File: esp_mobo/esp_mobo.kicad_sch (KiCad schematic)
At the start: 62 parts, among them J1 Conn_01x04_Pin, J10 Conn_01x03_Pin, J11 Conn_01x03_Pin, J12 Conn_01x03_Pin, J13 Conn_01x03_Pin, J14 Conn_01x03_Pin, J15 Conn_01x03_Pin, J2 Screw_Terminal_01x02, J3 Conn_01x03_Pin, J4 Conn_01x03_Pin, J5 Conn_01x03_Pin, J6 Conn_01x03_Pin, J7 Conn_01x03_Pin, J8 Conn_01x03_Pin, J9 Conn_01x03_Pin, U1 ESP32-DevKitC, U2 74AHCT125, U3 PC847, U4 PC847, U5 BME280

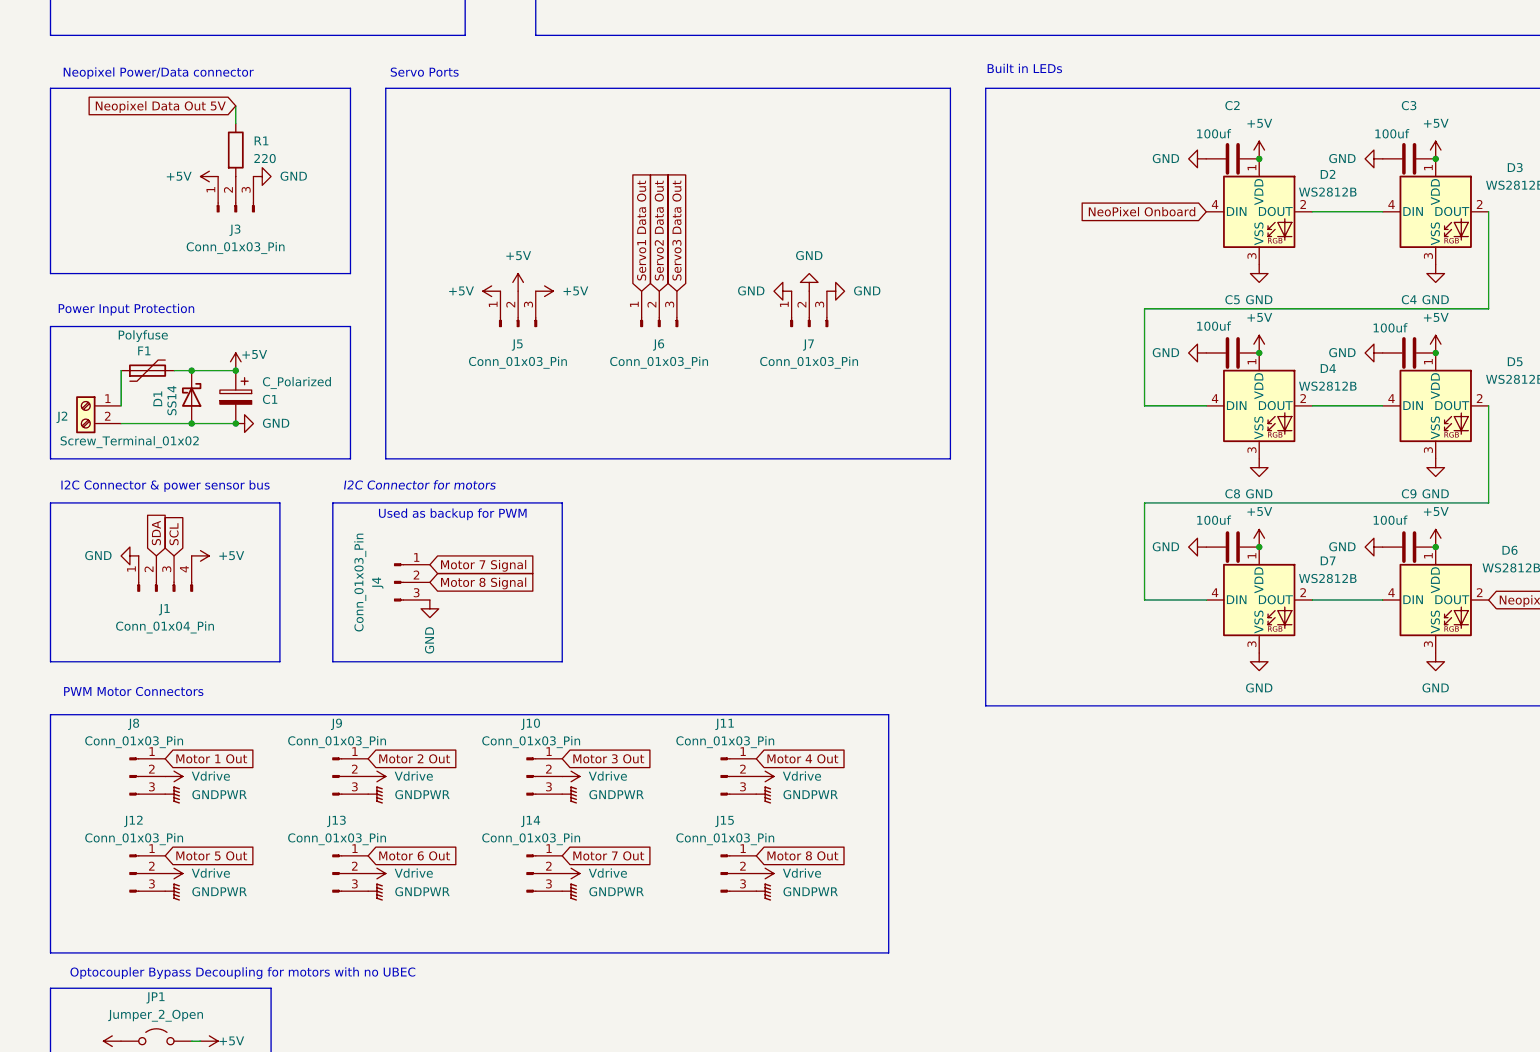
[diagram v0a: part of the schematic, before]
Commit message: Update ESC Mobo Silkscreen
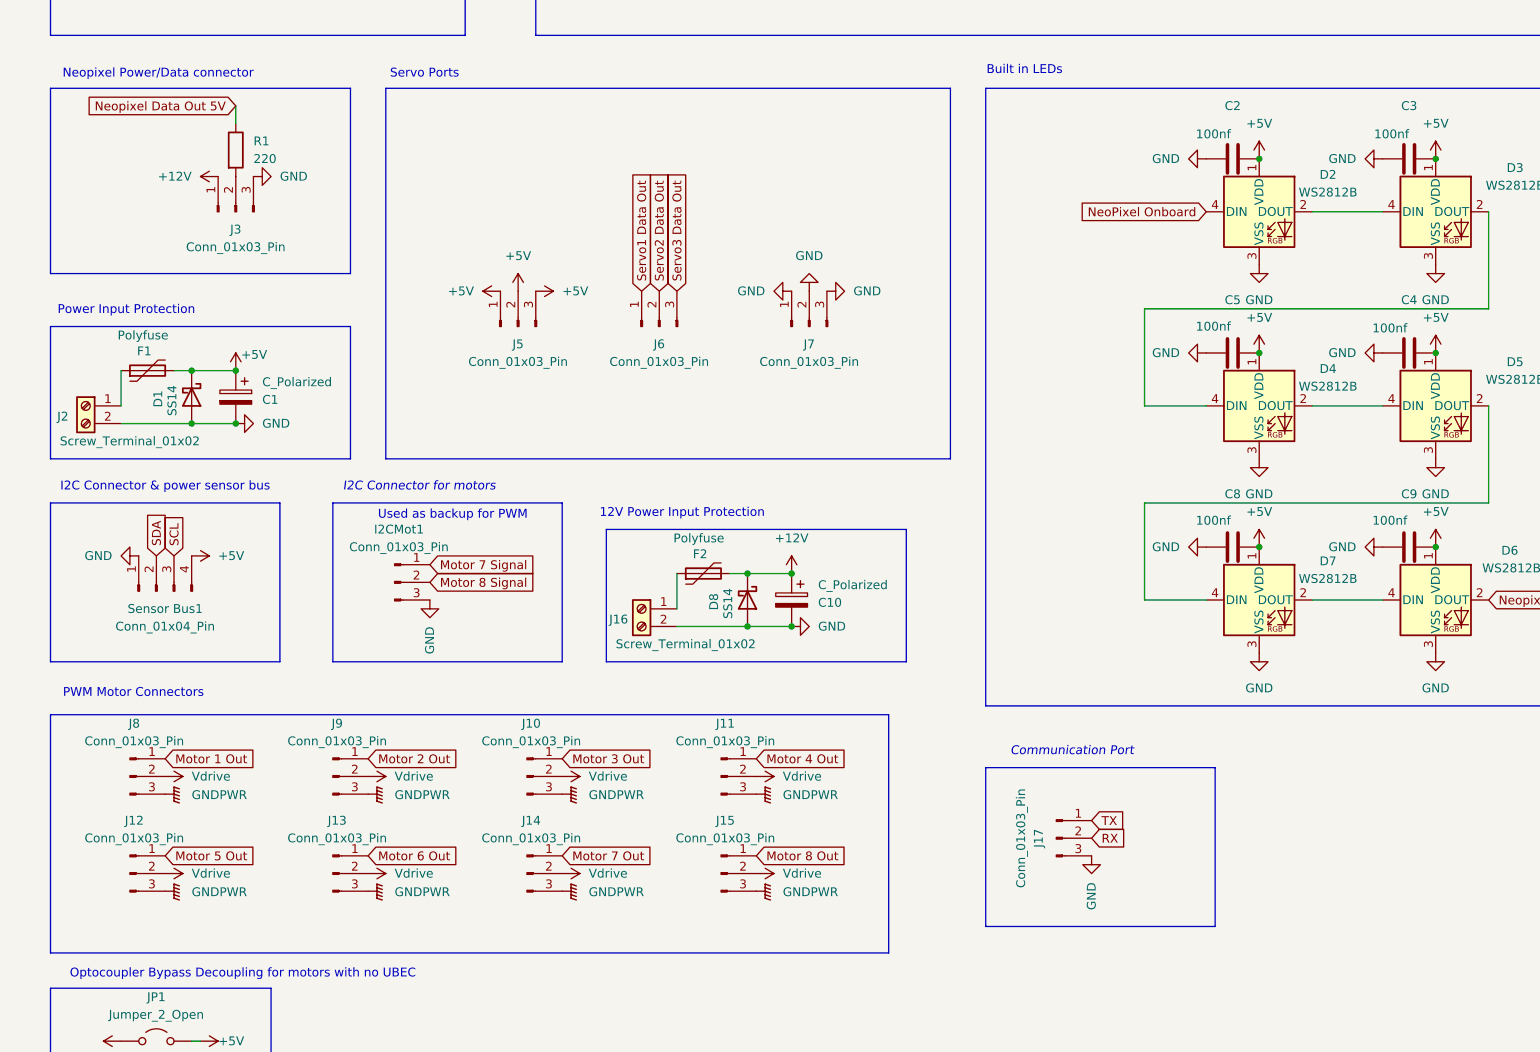
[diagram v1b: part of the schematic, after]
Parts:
- added C10: C_Polarized, Capacitor_THT:CP_Radial_D5.0mm_P2.00mm, symbol Device:C_Polarized
- added D8: SS14, Diode_SMD:D_SMA, symbol Diode:SS14
- added F2: Polyfuse, Fuse:Fuse_Bourns_MF-RG300, symbol Device:Polyfuse
- added J16: Screw_Terminal_01x02, TerminalBlock_TE-Connectivity:TerminalBlock_TE_282834-2_1x02_P2.54mm_Horizontal, symbol Connector:Screw_Terminal_01x02
- added J17: Conn_01x03_Pin, Connector_JST:JST_XH_B3B-XH-AM_1x03_P2.50mm_Vertical, symbol Connector:Conn_01x03_Pin
- C2, C3, C4, C5, C8, C9: value 100uf -> 100nf
- C6, C7: footprint (none) -> Capacitor_SMD:C_0603_1608Metric_Pad1.08x0.95mm_HandSolder
- JP1: footprint (none) -> Connector_PinHeader_2.54mm:PinHeader_1x02_P2.54mm_Vertical
- R18, R19: footprint (none) -> Resistor_SMD:R_0603_1608Metric_Pad0.98x0.95mm_HandSolder
- Sensor Bus1: renamed from J1
- renumbered J4 to I2CMot1
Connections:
- net +5V: no longer J3.1 (Pin_1)
- net GND: now also C10.2, D8.2 (A), J16.2 (Pin_2), J17.3 (Pin_3)
- net RX: now also J17.2 (Pin_2)
- net TX: now also J17.1 (Pin_1)
- new net: F2.1, J16.1 (Pin_1)
- new net +12V: C10.1, D8.1 (K), F2.2, J3.1 (Pin_1)
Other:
- note added: "12V Power Input Protection"
- note added: "Communication Port"

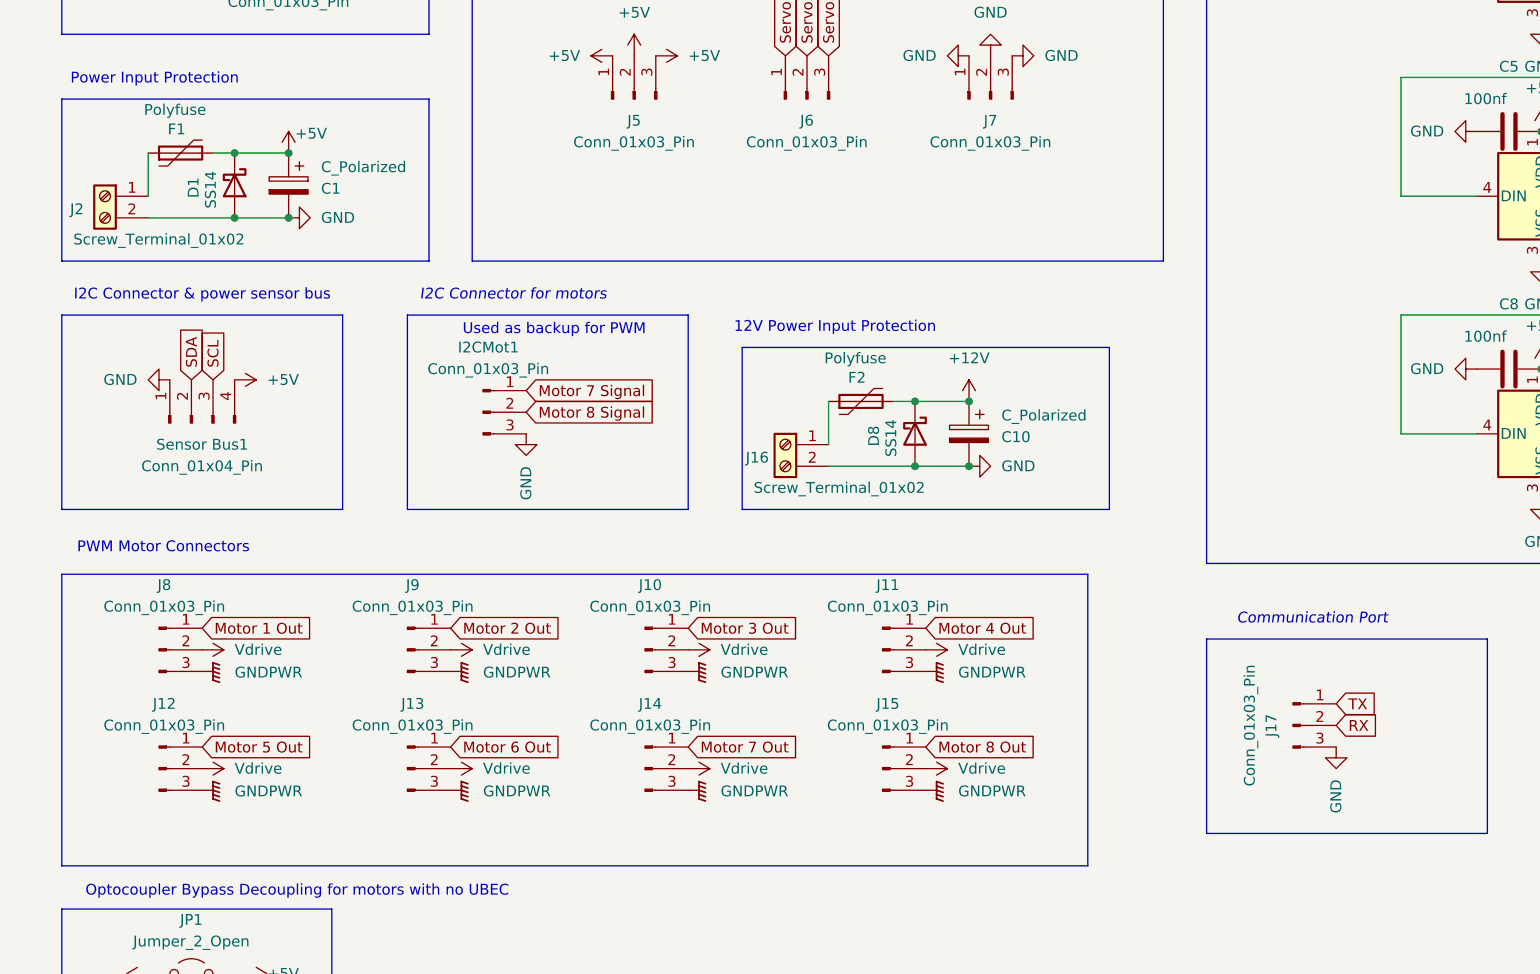
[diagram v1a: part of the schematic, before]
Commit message: Update ESC Mobo Ground Points
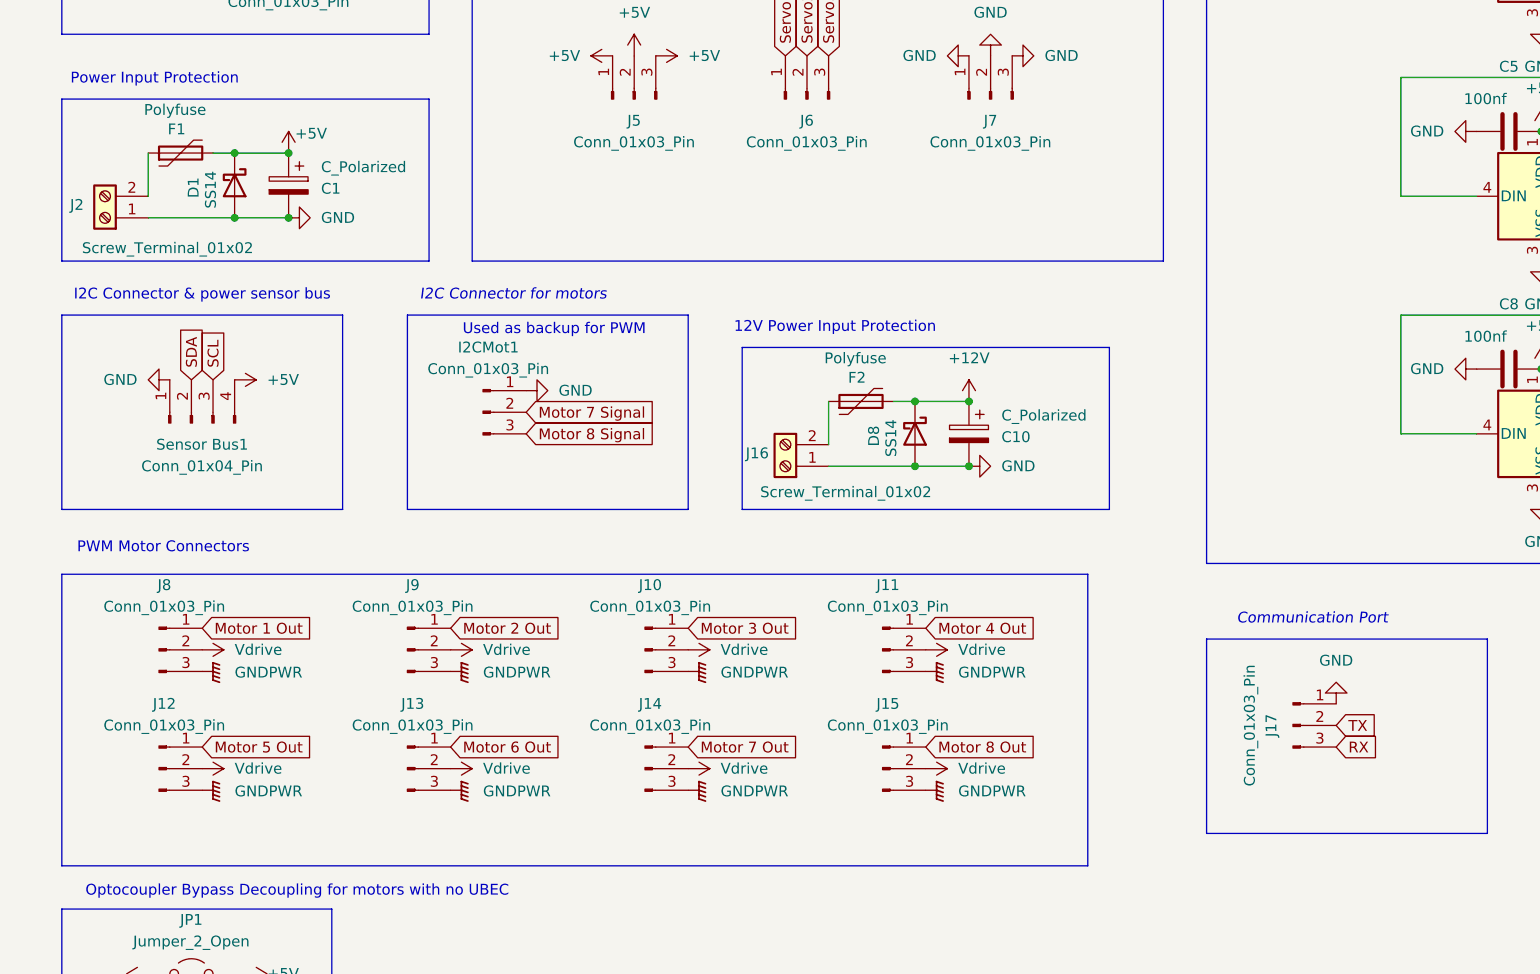
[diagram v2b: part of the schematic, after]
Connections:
- net GND: now also I2CMot1.1 (Pin_1), J16.1 (Pin_1), J17.1 (Pin_1), J2.1 (Pin_1); no longer I2CMot1.3 (Pin_3), J16.2 (Pin_2), J17.3 (Pin_3), J2.2 (Pin_2)
- net Motor 7 Signal: now also I2CMot1.2 (Pin_2); no longer I2CMot1.1 (Pin_1)
- net Motor 8 Signal: now also I2CMot1.3 (Pin_3); no longer I2CMot1.2 (Pin_2)
- net RX: now also J17.3 (Pin_3); no longer J17.2 (Pin_2)
- net TX: now also J17.2 (Pin_2); no longer J17.1 (Pin_1)
- net at F1.1: now also J2.2 (Pin_2); no longer J2.1 (Pin_1)
- net at F2.1: now also J16.2 (Pin_2); no longer J16.1 (Pin_1)
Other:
- moved on the sheet: J16, J2

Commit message: Lots of changes
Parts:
- added R20, R25: 20K, Resistor_SMD:R_0603_1608Metric_Pad0.98x0.95mm_HandSolder, symbol Device:R
- added R21, R22, R23, R24: 10K, Resistor_SMD:R_0603_1608Metric_Pad0.98x0.95mm_HandSolder, symbol Device:R
- added U6, U8: TMCS1100A2QDR, SOIC8_D_TEX, symbol TMCS1100A2QDR:TMCS1100A2QDR
- added U7, U9: LM4030-2.5, Package_TO_SOT_SMD:SOT-23-5, symbol Reference_Voltage:LM4030-2.5
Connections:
- net +12V: now also U6.1 (IN+), U6.2 (IN+); no longer J3.1 (Pin_1)
- net +3.3V: now also R21.1, R22.2, R23.2, R24.2
- net +5V: now also R20.1, R25.1, U6.8 (VS), U8.3 (IN-), U8.4 (IN-), U8.8 (VS); no longer C1.1, D1.1 (K), F1.2
- net GND: now also U6.5 (GND), U7.5 (A), U8.5 (GND), U9.5 (A)
- net Motor 7 Signal: now also R24.1
- net Motor 8 Signal: now also R23.1
- net SCL: now also R22.1
- net SDA: now also R21.2
- net CurrentSensNeoPix: now reaches U1.5 (VDET_1/GPIO34/ADC1_CH6)
- net CurrentSensNeoPix: now also U6.7 (VOUT)
- net CurrentSens5V: now reaches U1.6 (VDET_2/GPIO35/ADC1_CH7)
- net CurrentSens5V: now also U8.7 (VOUT)
- new net: R25.2, U8.6 (VREF), U9.4 (K)
- new net: R20.2, U6.6 (VREF), U7.4 (K)
- new net 5VInput: C1.1, D1.1 (K), F1.2, U8.1 (IN+), U8.2 (IN+)
- new net NeoPowerOut: J3.1 (Pin_1), U6.3 (IN-), U6.4 (IN-)
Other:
- moved on the sheet: I2CMot1, Sensor Bus1

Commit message: Add leak sensor
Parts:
- added C11, C12: 0.1uF, Capacitor_SMD:C_0603_1608Metric, symbol Device:C
- added R26: 20K, Resistor_SMD:R_0603_1608Metric_Pad0.98x0.95mm_HandSolder, symbol Device:R
- added U10: BMI088, QFN_BMI085_BOS, symbol BMI088:BMI088
- added U11: TMCS1100A2QDR, SOIC8_D_TEX, symbol TMCS1100A2QDR:TMCS1100A2QDR
- added U12: LM4030-2.5, Package_TO_SOT_SMD:SOT-23-5, symbol Reference_Voltage:LM4030-2.5
- J10, J11, J12, J13, J14, J15, J5, J6, J7, J8, J9: footprint Connector_PinHeader_2.54mm:PinHeader_1x03_P2.54mm_Vertical -> ConnectorSmallCourtyard:PinHeader_1x03_P2.54mm_Vertical_small_courtyard
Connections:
- net +12V: now also U11.3 (IN-), U11.4 (IN-); no longer C10.1, D8.1 (K), F2.2
- net +3.3V: now also C11.1, C12.1, U10.11 (VDDIO), U10.14 (CSB1), U10.3 (VDD), U10.7 (PS)
- net +5V: now also R26.1, U11.8 (VS)
- net GND: now also C11.2, C12.2, U10.4 (GNDA), U10.6 (GNDIO), U11.5 (GND), U12.5 (A); no longer H1.1, H2.1, H3.1, H4.1
- net SCL: now also U10.8 (SCL/SCK)
- net SDA: now also U10.9 (SDA/SDI)
- net CurrentSens12V: now reaches U1.9 (DAC_1/ADC2_CH8/GPIO25)
- net CurrentSens12V: now also U11.7 (VOUT)
- new net: R26.2, U11.6 (VREF), U12.4 (K)
- new net 12VInput: C10.1, D8.1 (K), F2.2, U11.1 (IN+), U11.2 (IN+)
- no-connect marks 6 -> 17
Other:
- moved on the sheet: R20, R25, U6, U7, U8, U9
